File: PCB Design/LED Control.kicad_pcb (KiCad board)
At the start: 2 copper layers, 7 x 7 mm, 25 parts, among them J1 5V 5A Power, J2 TO WS2812B LED STRIP, J3 Conn_01x03, SW1 SW_Push_Dual

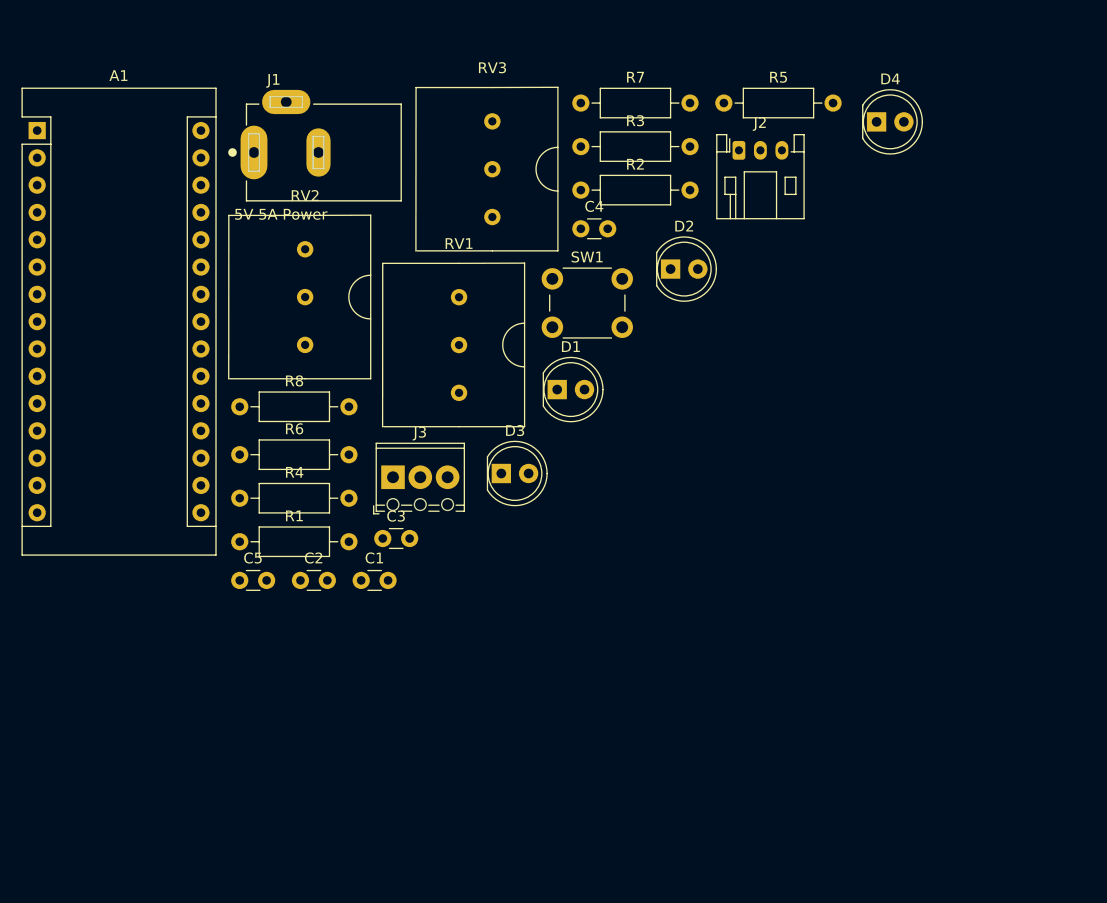
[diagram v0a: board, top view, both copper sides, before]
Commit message: capacitor footprints changed to axial
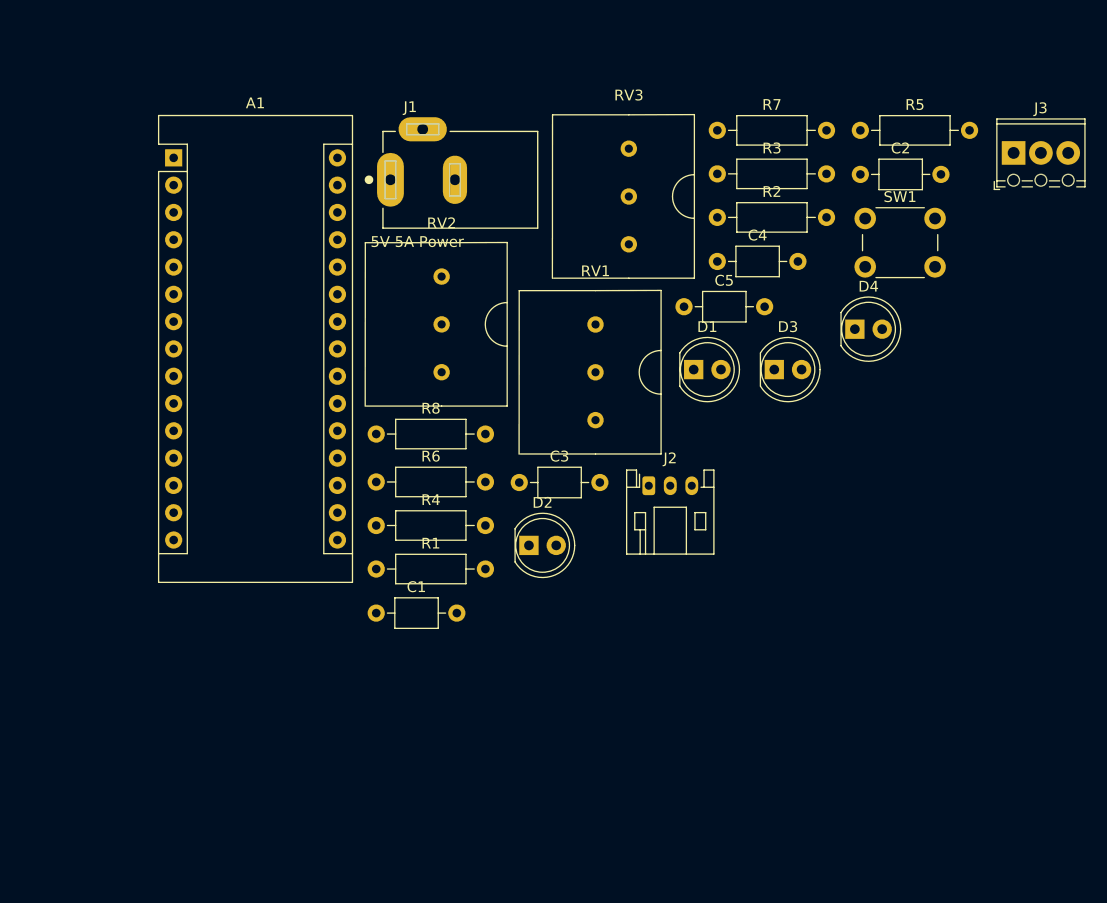
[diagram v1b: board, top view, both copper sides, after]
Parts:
- C1, C2, C3, C4, C5: footprint Capacitor_THT:C_Disc_D3.0mm_W1.6mm_P2.50mm -> Capacitor_THT:C_Axial_L3.8mm_D2.6mm_P7.50mm_Horizontal
- moved J3 65.2 mm to (181.3, 72.2)
- moved C2 64.4 mm to (167.1, 74.2)
- moved C5 48.6 mm to (150.6, 86.5)
- moved J2 32.3 mm to (147.4, 103.2)
- moved SW1 29.6 mm to (167.5, 78.3)
- moved D2 28.9 mm to (136.2, 108.7)
- moved D3 27.2 mm to (159.0, 92.4)
- moved D4 19.4 mm to (166.5, 88.6)
- moved C3 13.7 mm to (135.3, 102.9)
- moved C4 13.1 mm to (153.7, 82.3)
- moved R5 13.0 mm to (167.1, 70.1)
- moved A1 13.0 mm to (103.2, 72.7)
- moved J1 13.0 mm to (123.3, 74.7)
- moved RV2 13.0 mm to (128.1, 88.2)
- moved R6 13.0 mm to (122.0, 102.8)
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
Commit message: Rs, Cs, LED updated for SMT
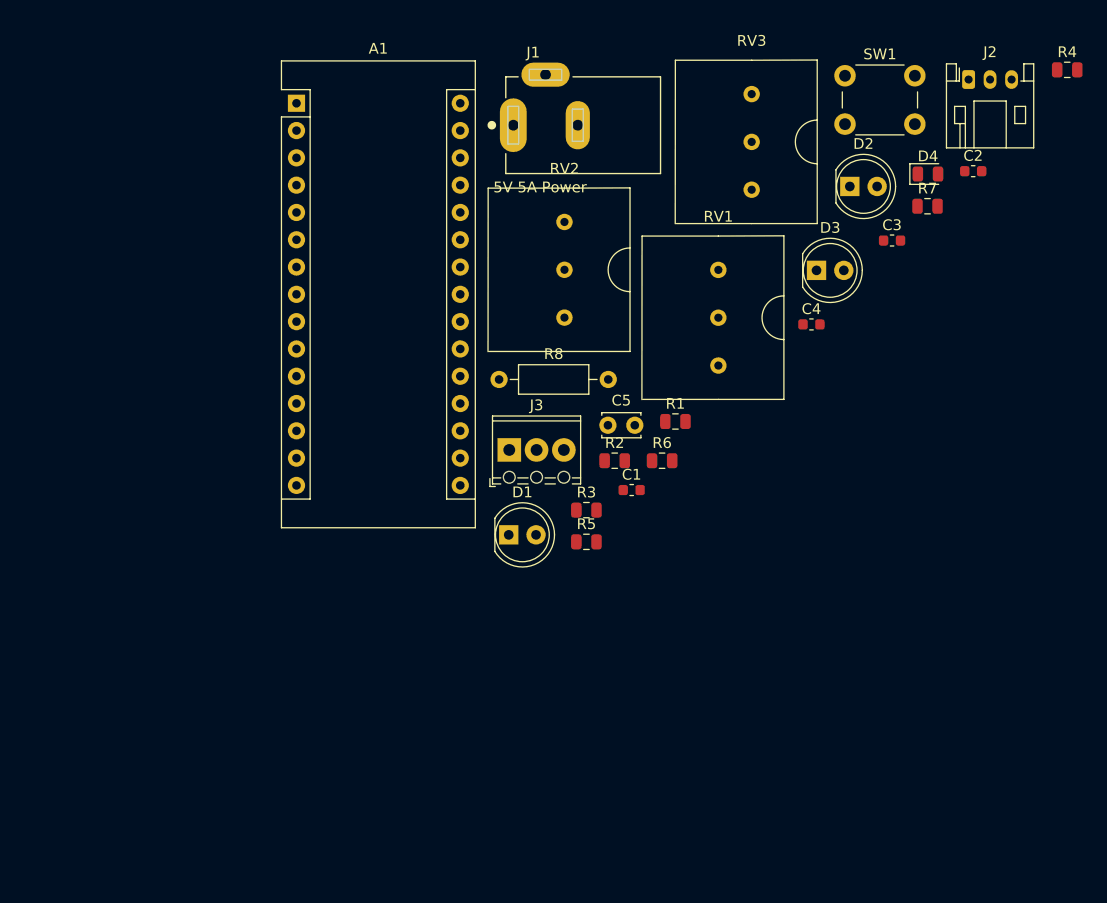
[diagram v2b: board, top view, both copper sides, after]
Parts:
- C1, C2, C3, C4: footprint Capacitor_THT:C_Axial_L3.8mm_D2.6mm_P7.50mm_Horizontal -> Capacitor_SMD:C_0603_1608Metric
- C5: footprint Capacitor_THT:C_Axial_L3.8mm_D2.6mm_P7.50mm_Horizontal -> Capacitor_THT:C_Disc_D3.4mm_W2.1mm_P2.50mm
- D4: footprint LED_THT:LED_D5.0mm -> LED_SMD:LED_0805_2012Metric
- R1, R2, R3, R4, R5, R6: footprint Resistor_THT:R_Axial_DIN0207_L6.3mm_D2.5mm_P10.16mm_Horizontal -> Resistor_SMD:R_0805_2012Metric
- R7: value 330 -> 100; footprint Resistor_THT:R_Axial_DIN0207_L6.3mm_D2.5mm_P10.16mm_Horizontal -> Resistor_SMD:R_0805_2012Metric
- moved R4 77.0 mm to (186.3, 64.5)
- moved J3 54.5 mm to (134.4, 99.8)
- moved J2 48.1 mm to (177.1, 65.4)
- moved R5 46.0 mm to (141.6, 108.4)
- moved D2 44.8 mm to (166.1, 75.3)
- moved C3 41.4 mm to (170.0, 80.4)
- moved R3 33.6 mm to (141.6, 105.4)
- moved R1 31.0 mm to (149.8, 97.2)
- moved R6 26.7 mm to (148.6, 100.8)
- moved C1 26.4 mm to (145.8, 103.6)
- moved R2 24.6 mm to (144.2, 100.8)
- moved D1 23.1 mm to (134.3, 107.7)
- moved R7 20.8 mm to (173.3, 77.2)
- moved D4 16.0 mm to (173.3, 74.2)
- moved SW1 13.4 mm to (165.6, 65.0)
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
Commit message: pcb layout created
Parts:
- added R9: 10k, Resistor_SMD:R_0805_2012Metric, F.Cu at (111.3, 117.3)
- J2: footprint Connector_JST:JST_PH_S3B-PH-K_1x03_P2.00mm_Horizontal -> TerminalBlock_Phoenix:TerminalBlock_Phoenix_MPT-0,5-3-2.54_1x03_P2.54mm_Horizontal
- J3: value Conn_01x03 -> Sound Sensor
- R1, R6: value 1k -> 10k
- R8: footprint Resistor_THT:R_Axial_DIN0207_L6.3mm_D2.5mm_P10.16mm_Horizontal -> Resistor_SMD:R_0805_2012Metric
- moved J2 98.6 mm to (99.3, 126.0)
- moved R4 77.9 mm to (109.7, 78.7), turned to 180 degrees
- moved C2 72.8 mm to (112.3, 106.2), turned to 90 degrees
- moved D2 65.3 mm to (101.1, 81.3), turned to 90 degrees
- moved D3 62.2 mm to (101.1, 89.2), turned to 90 degrees
- moved J1 51.3 mm to (102.1, 109.2), turned to 90 degrees
- moved D1 47.8 mm to (101.1, 73.4), turned to 90 degrees
- moved R3 46.2 mm to (111.3, 70.6), turned to 180 degrees
- moved R2 45.2 mm to (102.1, 117.3), turned to 90 degrees
- moved R5 38.4 mm to (110.0, 86.6), turned to 180 degrees
- moved SW1 38.1 mm to (129.0, 75.7), turned to 180 degrees
- moved R6 36.4 mm to (112.3, 99.6), turned to 90 degrees
- moved RV1 35.8 mm to (163.8, 121.9)
- moved C3 33.2 mm to (137.7, 72.6)
- moved C5 32.4 mm to (116.8, 115.8), turned to 270 degrees
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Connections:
- R1 pad 1: VCC -> +5V
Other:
- outline, holes or cut-outs redrawn

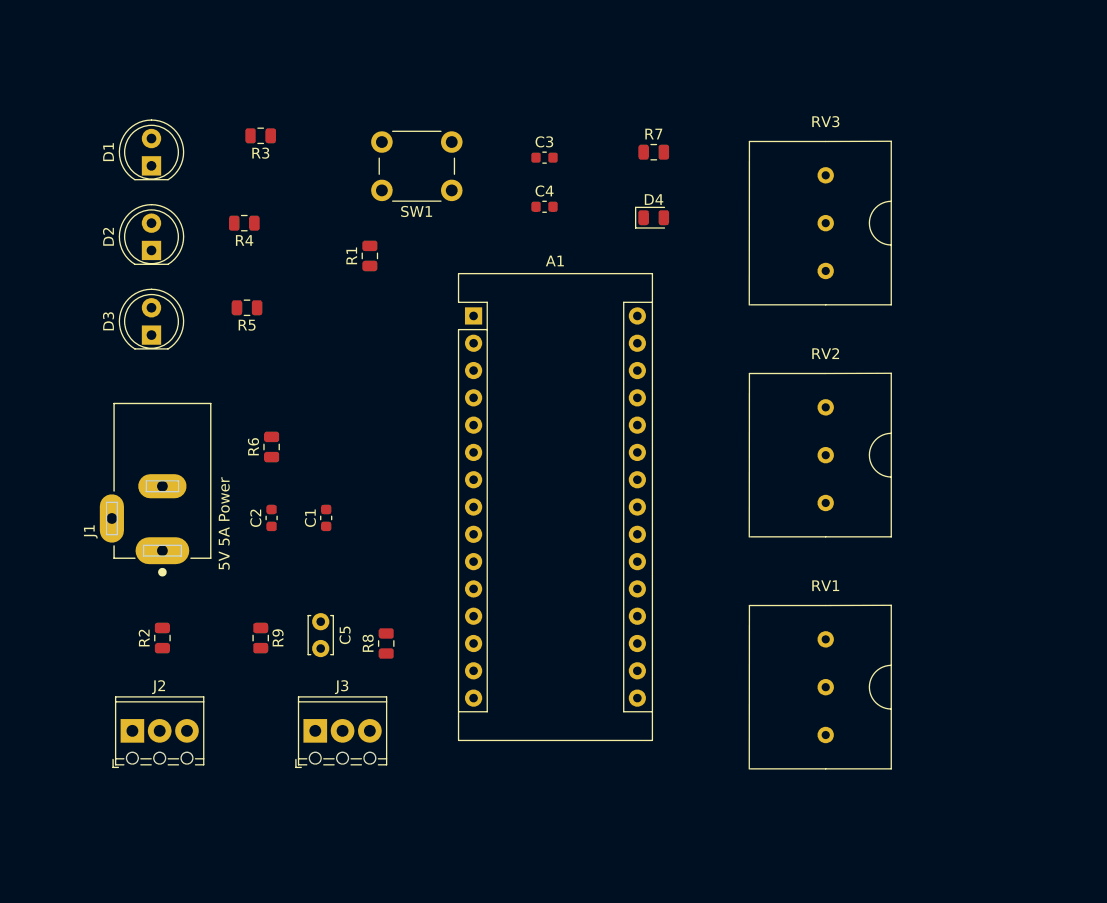
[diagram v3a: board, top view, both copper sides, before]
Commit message: pcb size made 60x60
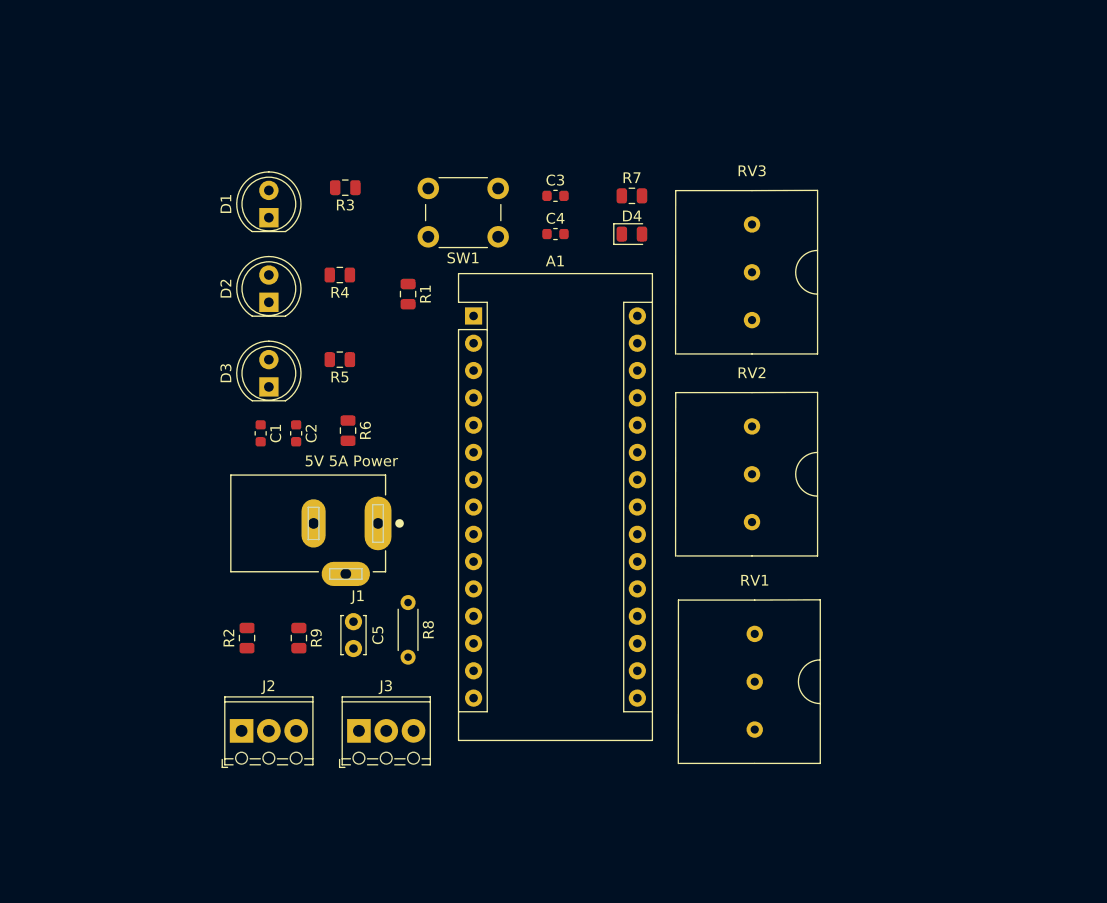
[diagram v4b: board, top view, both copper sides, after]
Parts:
- R8: footprint Resistor_SMD:R_0805_2012Metric -> Resistor_THT:R_Axial_DIN0204_L3.6mm_D1.6mm_P5.08mm_Horizontal
- moved J1 20.2 mm to (122.2, 106.7), turned to 180 degrees
- moved D3 11.9 mm to (112.0, 94.0)
- moved D1 11.9 mm to (112.0, 78.2)
- moved D2 11.9 mm to (112.0, 86.1)
- moved J2 10.2 mm to (109.5, 126.0)
- moved R4 10.1 mm to (118.6, 83.6)
- moved C1 9.96 mm to (111.3, 98.3), turned to 270 degrees
- moved R5 9.89 mm to (118.6, 91.4)
- moved R3 9.24 mm to (119.1, 75.4)
- moved RV3 8.24 mm to (157.0, 83.3)
- moved C2 8.20 mm to (114.6, 98.3), turned to 270 degrees
- moved R2 7.87 mm to (110.0, 117.3)
- moved R6 7.27 mm to (119.4, 98.0), turned to 270 degrees
- moved RV2 7.08 mm to (157.0, 102.1)
- moved RV1 6.62 mm to (157.2, 121.4)
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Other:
- board size 7 x 7 mm -> 7 x 6.9 mm

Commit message: edge cuts and M3 mounting holes added
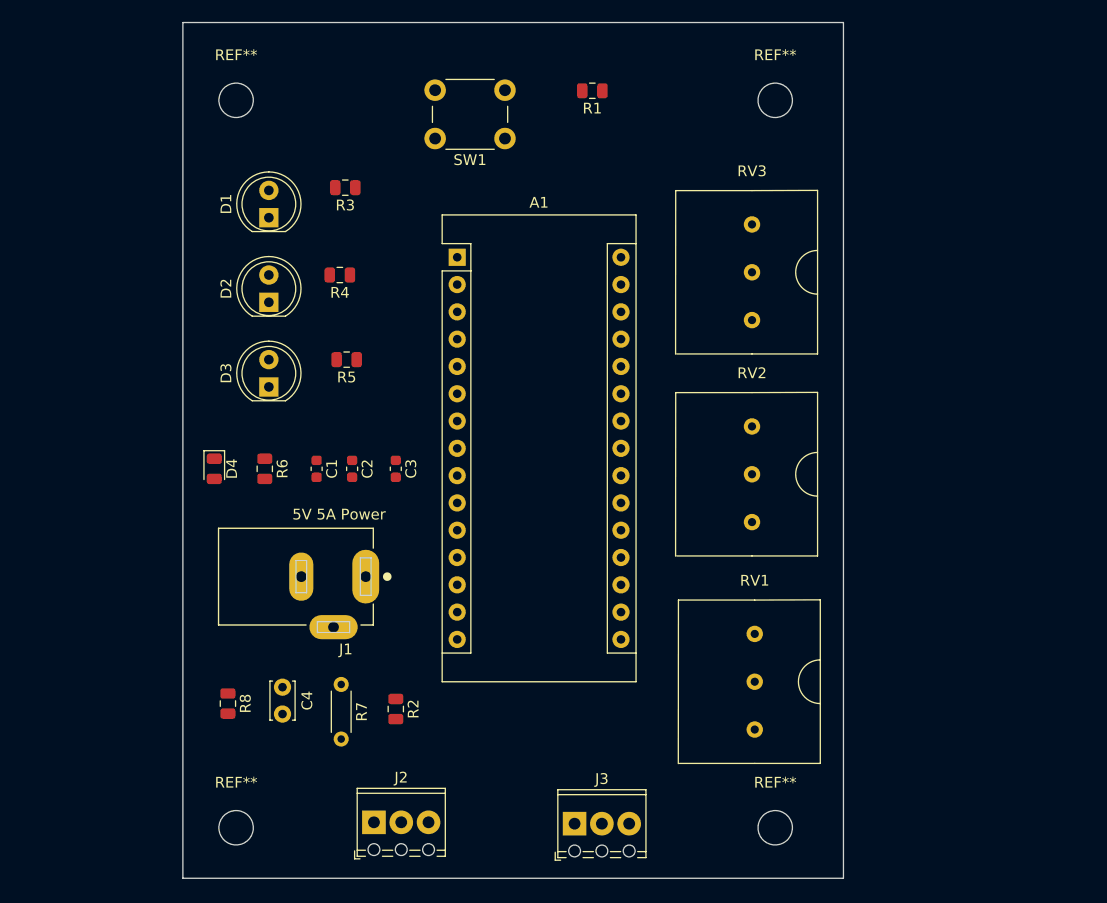
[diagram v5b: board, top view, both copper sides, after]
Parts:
- removed C5: 0.1uF, Capacitor_THT:C_Disc_D3.4mm_W2.1mm_P2.50mm
- removed the R6 at (119.4, 98.0)
- removed R9: 10k, Resistor_SMD:R_0805_2012Metric
- added R8: 10k, Resistor_SMD:R_0805_2012Metric, F.Cu at (108.2, 123.4)
- added REF**: MountingHole_3.2mm_M3, MountingHole:MountingHole_3.2mm_M3, F.Cu at (109.0, 135.0)
- added REF**: MountingHole_3.2mm_M3, MountingHole:MountingHole_3.2mm_M3, F.Cu at (159.1, 135.0)
- added REF**: MountingHole_3.2mm_M3, MountingHole:MountingHole_3.2mm_M3, F.Cu at (109.0, 67.3)
- added REF**: MountingHole_3.2mm_M3, MountingHole:MountingHole_3.2mm_M3, F.Cu at (159.1, 67.3)
- C4: value 1uF -> 0.1uF; footprint Capacitor_SMD:C_0603_1608Metric -> Capacitor_THT:C_Disc_D3.4mm_W2.1mm_P2.50mm
- moved C4 49.2 mm to (113.3, 121.9), turned to 270 degrees
- moved D4 44.6 mm to (106.9, 101.6), turned to 270 degrees
- moved R6 42.6 mm to (111.6, 101.6), turned to 270 degrees
- moved C3 29.4 mm to (123.8, 101.6), turned to 270 degrees
- moved R1 25.5 mm to (142.1, 66.4), turned to 180 degrees
- moved J3 21.8 mm to (140.5, 134.6)
- moved R2 15.3 mm to (123.8, 124.0), turned to 270 degrees
- moved J2 15.0 mm to (121.8, 134.5)
- moved R7 9.84 mm to (118.7, 121.7)
- moved SW1 9.17 mm to (134.0, 70.9)
- moved C1 6.17 mm to (116.5, 101.6)
- moved C2 6.17 mm to (119.8, 101.6)
- moved A1 5.67 mm to (129.5, 81.9)
- moved J1 5.08 mm to (121.0, 111.6)
- moved R5 0.64 mm to (119.3, 91.4)
- renumbered R7 to R6, R8 to R7
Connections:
- C1 pad 2: GNDPWR -> GND
- C2 pad 2: GNDPWR -> GND
- C3 pad 1: +5V -> VCC
- C4 pad 1: +5V -> A3
- J1 pad 2: GNDPWR -> GND
- J2 pad 3: GNDPWR -> GND
- J3 pad 3: +5V -> VCC
- R1 pad 1: +5V -> VCC
- R6 pad 1: +5V -> VCC
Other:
- board size 7 x 6.9 mm -> 61.5 x 79.6 mm

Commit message: microcontroller moved to bottom side
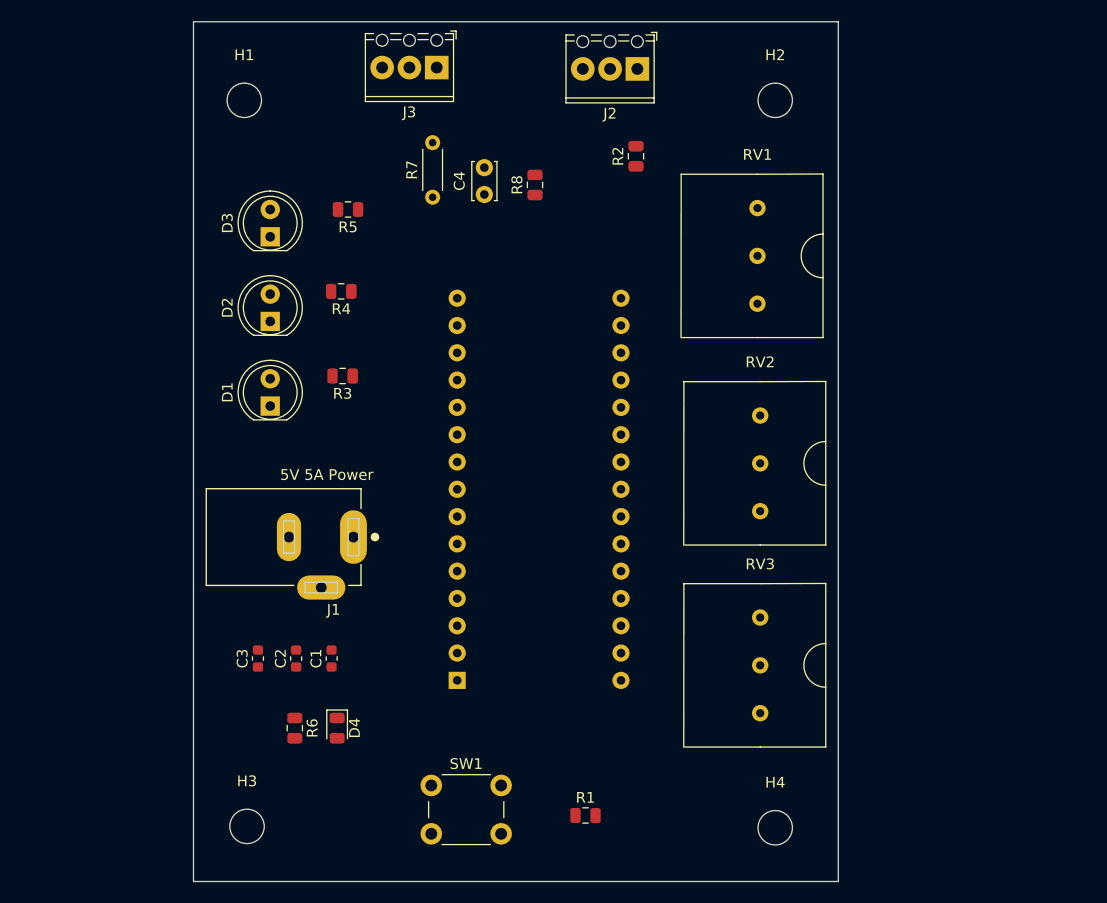
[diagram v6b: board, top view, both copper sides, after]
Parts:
- A1: moved to B.Cu
- moved J2 74.3 mm to (146.3, 64.4), turned to 180 degrees
- moved J3 71.5 mm to (127.6, 64.3), turned to 180 degrees
- moved R1 67.4 mm to (141.5, 133.9), turned to 0 degrees
- moved SW1 60.6 mm to (127.1, 131.1), turned to 0 degrees
- moved R8 56.1 mm to (136.8, 75.2), turned to 90 degrees
- moved R2 56.1 mm to (146.2, 72.5), turned to 90 degrees
- moved C4 49.5 mm to (132.1, 76.1), turned to 90 degrees
- moved R7 46.1 mm to (127.3, 76.3), turned to 90 degrees
- moved RV1 39.6 mm to (157.5, 81.8)
- moved A1 39.4 mm to (129.5, 121.3)
- moved RV3 36.6 mm to (157.7, 119.9)
- moved D4 26.7 mm to (118.4, 125.7)
- moved R6 24.3 mm to (114.4, 125.7)
- moved C3 21.8 mm to (111.0, 119.3), turned to 90 degrees
- moved C2 18.4 mm to (114.6, 119.3), turned to 90 degrees
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- renumbered REF** to H1, REF** to H2, REF** to H3, REF** to H4
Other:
- board size 61.5 x 79.6 mm -> 60 x 80 mm
